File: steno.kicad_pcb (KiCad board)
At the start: 2 copper layers, 195.3 x 81 mm, 49 parts, among them SW1 MX_Switch, SW10 MX_Switch, SW11 MX_Switch, SW12 MX_Switch, SW13 MX_Switch, SW14 MX_Switch, SW15 MX_Switch, SW16 MX_Switch, SW17 MX_Switch, SW18 MX_Switch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

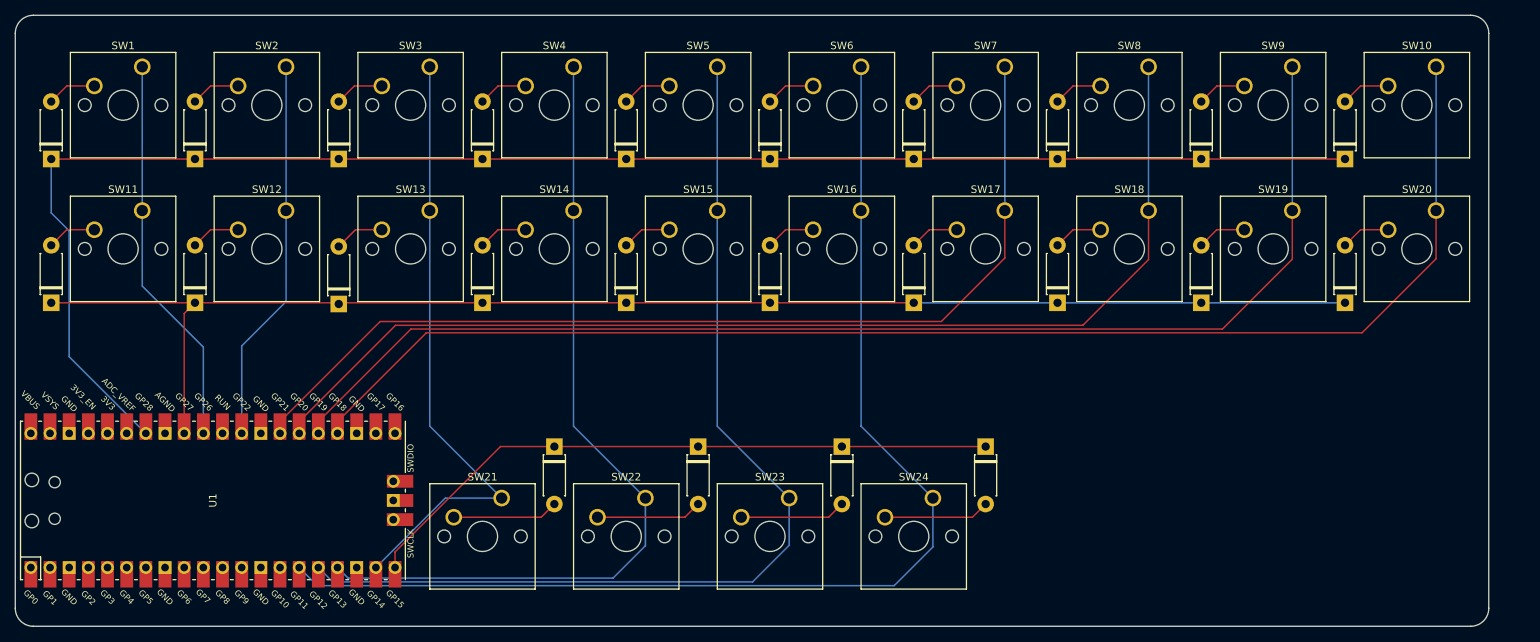
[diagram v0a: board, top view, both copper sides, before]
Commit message: Update PCB schematics to ECSKv2 design
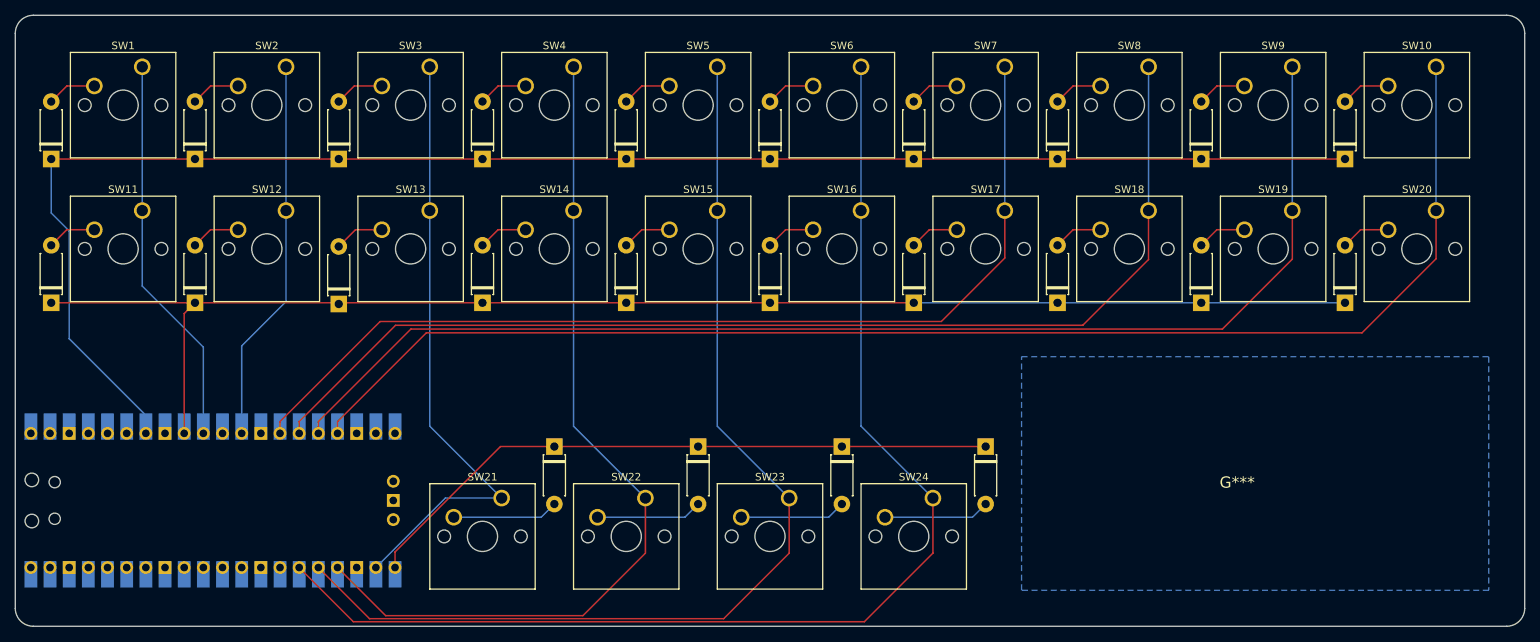
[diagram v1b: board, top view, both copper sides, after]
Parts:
- added G***: LOGO, LOGO, F.Cu at (176.2, 78.6)
- U1: moved to B.Cu
- turned U1 to -90 degrees
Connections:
- U1 pad 10: unconnected-(U1-GPIO7-Pad10) -> C1
- U1 pad 12: unconnected-(U1-GPIO9-Pad12) -> C2
- U1 pad 14: unconnected-(U1-GPIO10-Pad14) -> C7
- U1 pad 15: C6 -> C8
- U1 pad 16: C5 -> C9
- U1 pad 17: C4 -> C10
- U1 pad 19: C3 -> unconnected-(U1-GPIO14-Pad19)
- U1 pad 20: R3 -> unconnected-(U1-GPIO15-Pad20)
- U1 pad 21: unconnected-(U1-GPIO16-Pad21) -> R3
- U1 pad 22: unconnected-(U1-GPIO17-Pad22) -> C3
- U1 pad 24: C10 -> C4
- U1 pad 25: C9 -> C5
- U1 pad 26: C8 -> C6
- U1 pad 27: C7 -> unconnected-(U1-GPIO21-Pad27)
- U1 pad 29: C2 -> unconnected-(U1-GPIO22-Pad29)
- U1 pad 31: C1 -> unconnected-(U1-GPIO26_ADC0-Pad31)
- U1 pad 32: R2 -> unconnected-(U1-GPIO27_ADC1-Pad32)
- U1 pad 34: R1 -> unconnected-(U1-GPIO28_ADC2-Pad34)
- U1 pad 41: (no net) -> unconnected-(U1-SWCLK-Pad41)
- U1 pad 42: (no net) -> unconnected-(U1-GND-Pad42)
- U1 pad 43: (no net) -> unconnected-(U1-SWDIO-Pad43)
- U1 pad 7: unconnected-(U1-GPIO5-Pad7) -> R1
- U1 pad 9: unconnected-(U1-GPIO6-Pad9) -> R2
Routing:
- net C4: track 110.6 -> 115.3 mm
- net C5: track 132.5 -> 137.2 mm
- net C6: track 154.7 -> 159.1 mm
- added copper zone on B.Cu, net (none)
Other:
- board size 195.3 x 81 mm -> 200 x 81 mm
